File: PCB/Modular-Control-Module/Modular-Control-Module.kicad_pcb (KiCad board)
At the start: 4 copper layers, 59 x 49.4 mm, 40 parts, among them J1 Conn_ARM_SWD_TagConnect_TC203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, J2 DX07S016JA1R1500, SW1 B3U-1000P, SW2 B3U-1000P, T1 5051101092, U1 TEMPLATE, U2 RP2040, X1 ABM8G-12.000MHZ-18-D2Y-T

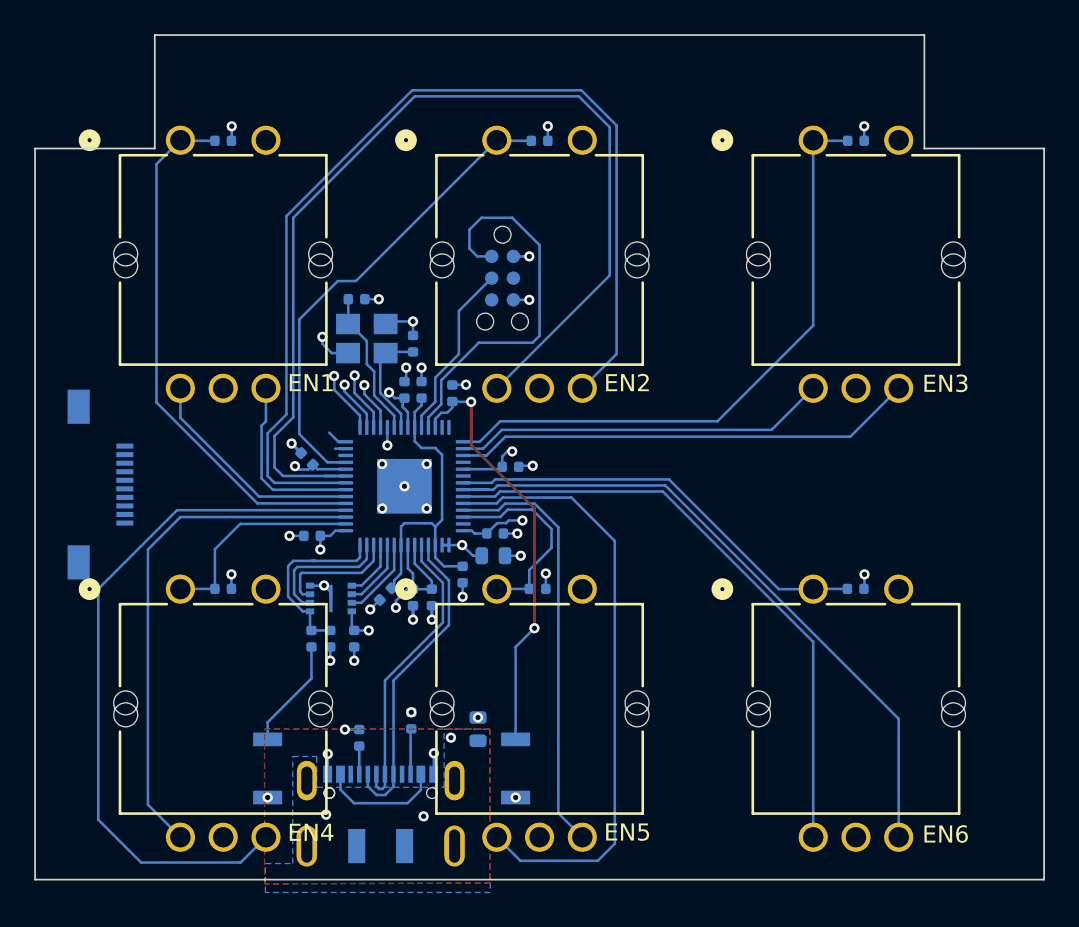
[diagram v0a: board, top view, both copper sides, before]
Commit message: Schematic Tweak and Board Route
Schaemtic and design tweaked to be SPI only. added more power pins for more current. Finished PCB route only needs to be put through DRC.
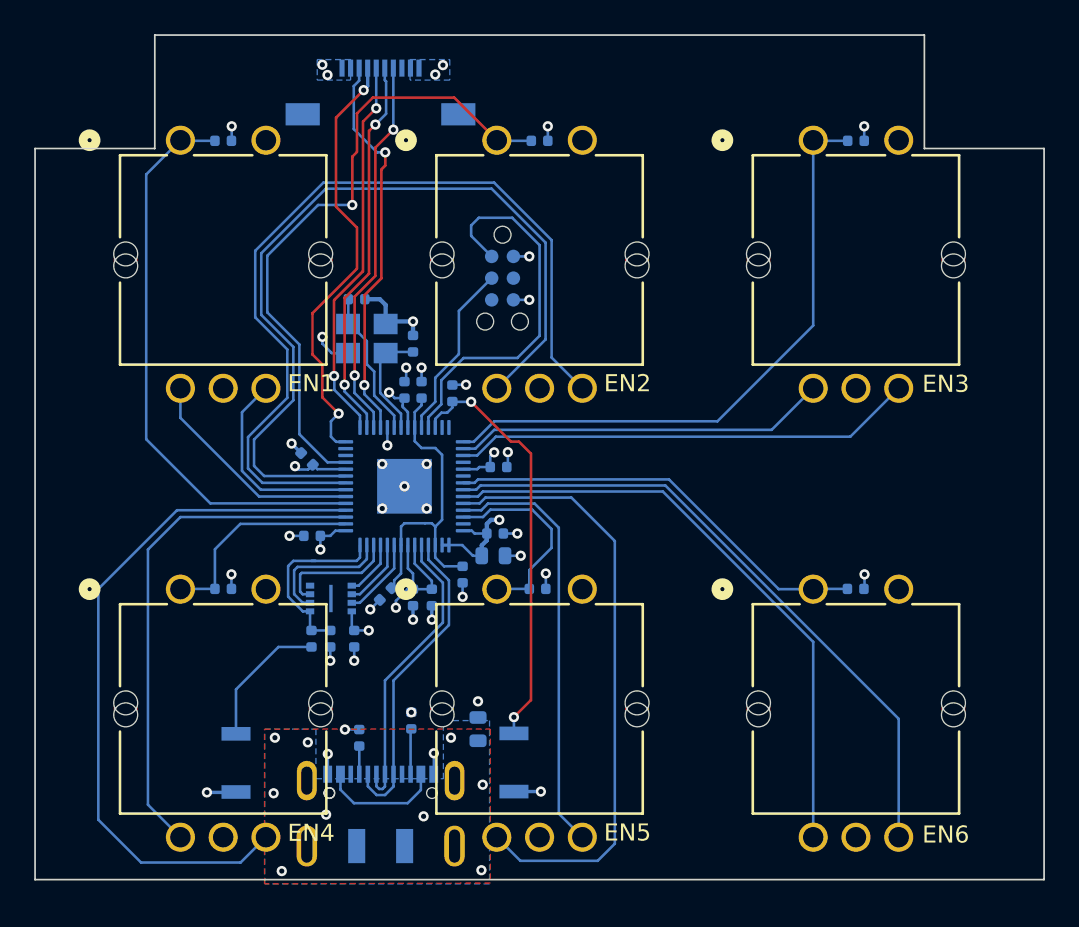
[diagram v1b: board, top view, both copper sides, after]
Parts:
- moved T1 28.0 mm to (97.7, 52.0), turned to 180 degrees
- moved SW1 1.88 mm to (89.2, 90.2)
- moved C13 0.70 mm to (104.6, 72.9)
- moved SW2 0.36 mm to (105.5, 90.2)
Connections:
- T1 pad 2: /I2C_SDA -> +3.3V
- T1 pad 3: /I2C_SCL -> unconnected-(T1-Pad3)
- T1 pad 4: /SLAVE_IRQ -> /SPI_MISO
- T1 pad 5: /SPI_SCK -> /SPI_CS
- T1 pad 6: /SPI_CS -> /SPI_SCK
- T1 pad 7: /SPI_MISO -> /SLAVE_IRQ
- U2 pad 12: /I2C_SDA -> unconnected-(U2-GPIO9-Pad12)
- U2 pad 13: /I2C_SCL -> unconnected-(U2-GPIO10-Pad13)
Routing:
- net /SLAVE_IRQ: track 1.19 -> 25.7 mm, vias 0 -> 2
- net /SPI_MOSI: track 2.88 -> 23.1 mm, vias 1 -> 2
- net /SPI_CS: track 3.04 -> 22.6 mm, vias 1 -> 2
- net /SPI_SCK: track 3.64 -> 22.7 mm, vias 1 -> 2
- net /SPI_MISO: track 3.50 -> 22.4 mm, vias 1 -> 2
- net /EN2_A: track 60.3 -> 49.0 mm
- net /EN2_S1: track 28.0 -> 37.9 mm, vias 0 -> 1
- net /EN2_B: track 59.8 -> 50.3 mm
- net GND: track 22.3 -> 25.5 mm
- net /EN1_S1: track 31.4 -> 33.5 mm
- net Net-(R2-Pad1): track 6.47 -> 8.04 mm
- net /EN1_B: track 10.6 -> 11.9 mm
- net /EN6_B: track 39.1 -> 38.1 mm
- net /I2C_SCL: track 0.62 -> 0.00 mm
- net +3.3V: track 37.3 -> 36.8 mm, vias 17 -> 18
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- added copper zone on B.Cu, net +3.3V
- added copper zone on B.Cu, net GND
